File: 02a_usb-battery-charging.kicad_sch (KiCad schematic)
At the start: 20 parts, among them J3 USB4105-GF-A, J4 Conn_01x02_Socket, J5 Conn_01x03_Socket, U1 USBLC6-2SC6, U2 BQ25170JDSGR

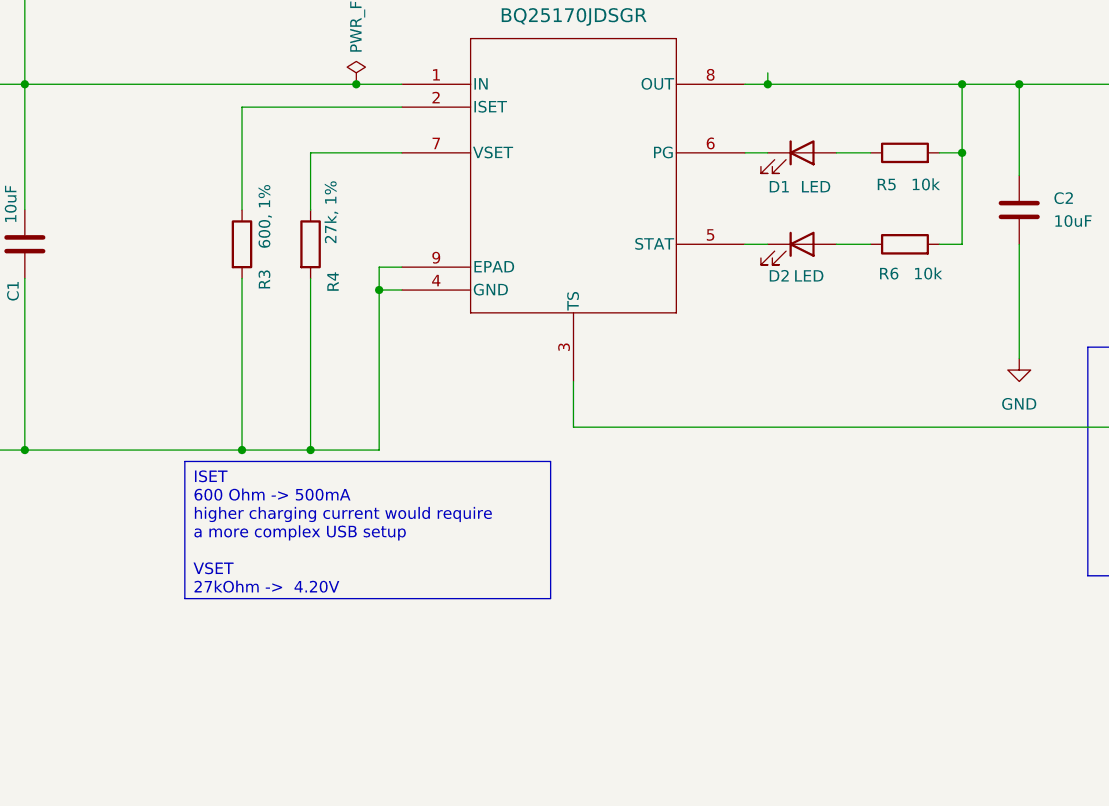
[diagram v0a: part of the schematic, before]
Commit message: Bigger Zener, improved BoM, general improvements
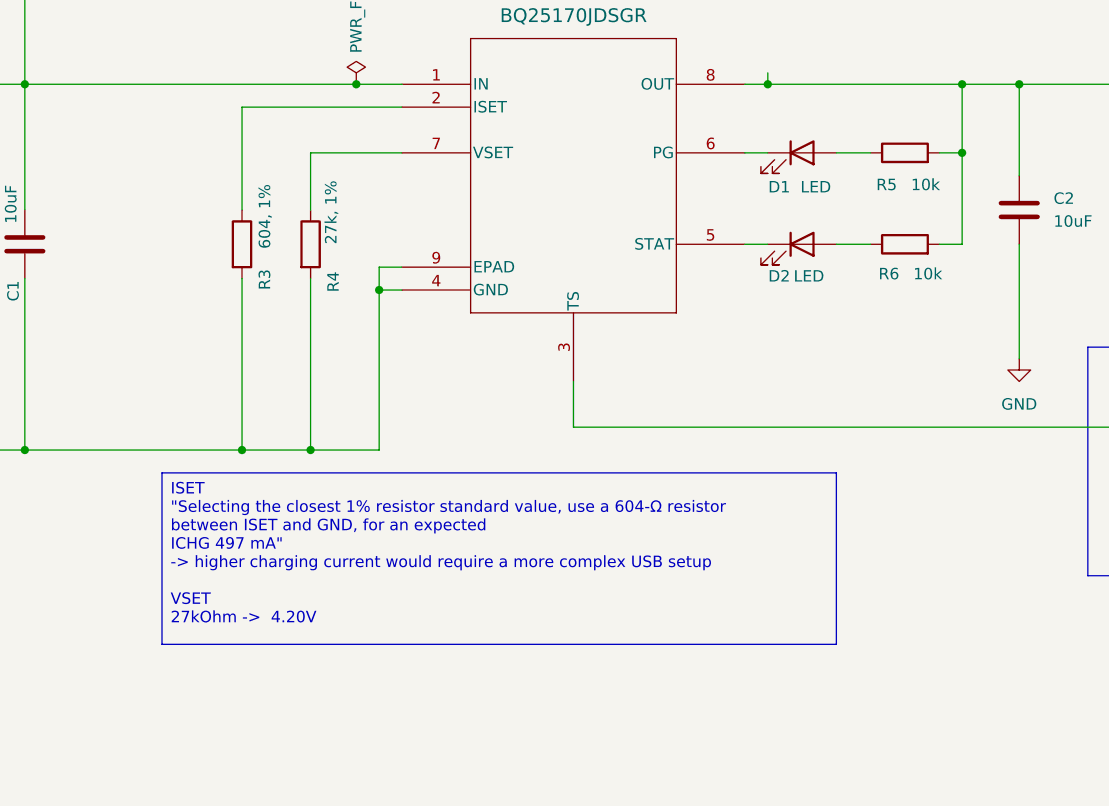
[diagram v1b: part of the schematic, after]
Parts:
- C1, C2: DigiKey (none) -> 1276-1804-1-ND; Manufacturer PartNo (none) -> CL31B106KAHNNNE
- D1: DigiKey (none) -> 732-4994-1-ND; Manufacturer PartNo (none) -> 150120YS75000
- D2: DigiKey (none) -> 732-4990-1-ND; Manufacturer PartNo (none) -> 150120GS75000
- F1: DigiKey (none) -> F3733CT-ND; Manufacturer PartNo (none) -> 1206L050/15YR
- J3: DigiKey (none) -> 2073-USB4105-GF-ACT-ND; Manufacturer PartNo (none) -> USB4105-GF-A
- J5: DigiKey (none) -> 455-1720-ND; Manufacturer PartNo (none) -> S3B-PH-K-S
- R1, R2: DigiKey (none) -> YAG3894CT-ND; Manufacturer PartNo (none) -> AC1206FR-075K1L
- R3: value 600, 1% -> 604, 1%; DigiKey (none) -> RNCP1206FTD604RCT-ND; Manufacturer PartNo (none) -> RNCP1206FTD604R
- R4: DigiKey (none) -> 311-27.0KFRCT-ND; Manufacturer PartNo (none) -> RC1206FR-0727KL
- R5, R6: DigiKey (none) -> 311-10.0KFRCT-ND; Manufacturer PartNo (none) -> RC1206FR-0710KL
- U1: Manufacturer PartNo (none) -> USBLC6-2SC6
- U2: DigiKey (none) -> 296-BQ25170JDSGRCT-ND; Manufacturer PartNo (none) -> BQ25170JDSGR

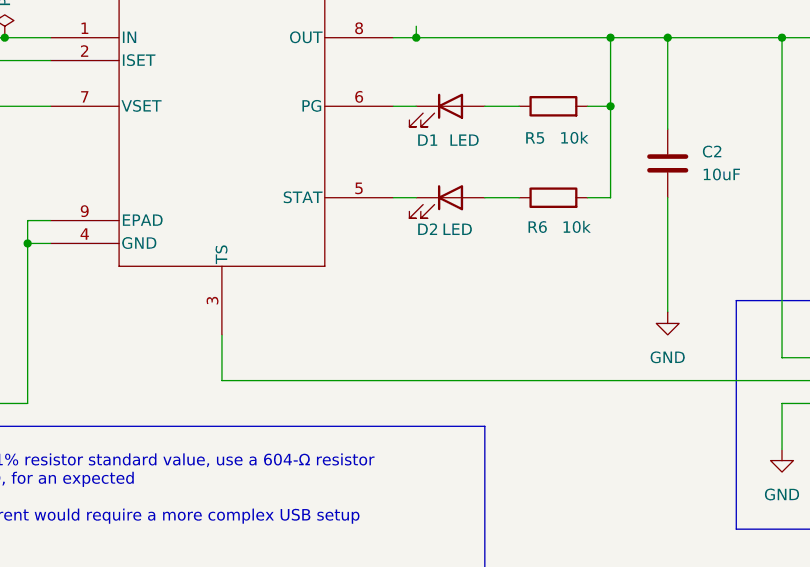
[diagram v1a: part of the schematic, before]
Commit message: Add proper charging detection, fix zener footprint
Connect the BQ25 status pin to the microcontroller for a proper
charging detection (low active).
Correct the footprint for the selected zener diode.
Somehow, the wrong footprint got assigned.
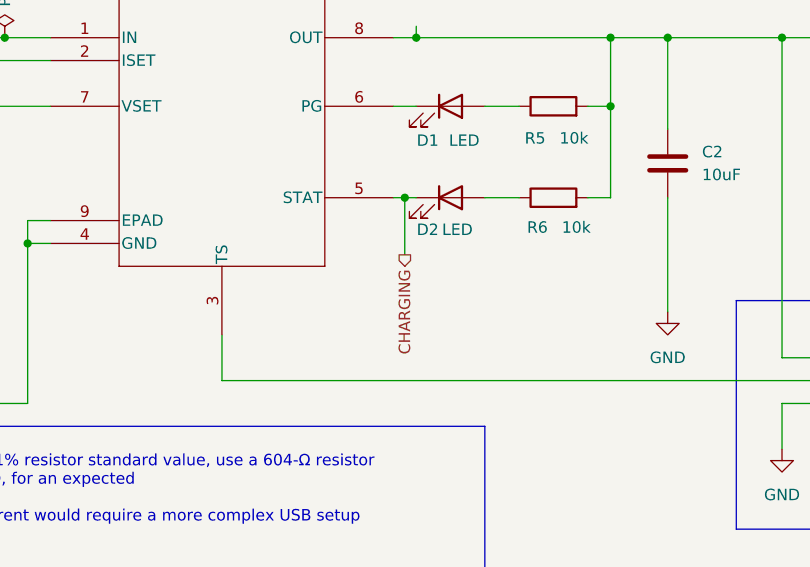
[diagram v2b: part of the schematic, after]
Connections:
- net CHARGING: now reaches D2.1 (K), U2.5 (STAT)
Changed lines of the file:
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@@
+	)
+	(junction
+		(at 189.23 93.98)
+		(diameter 0)
+		(color 0 0 0 0)
 	)
 	(junction
@@
 	(wire
 		(pts
+			(xy 189.23 93.98) (xy 190.5 93.98)
+		)
+		(stroke
+			(width 0)
+			(type default)
+		)
+	)
+	(wire
+		(pts
 			(xy 29.21 80.01) (xy 30.48 80.01)
 		)
@@
 	(wire
 		(pts
-			(xy 187.96 93.98) (xy 190.5 93.98)
+			(xy 187.96 93.98) (xy 189.23 93.98)
 		)
 		(stroke
@@
 		(pts
 			(xy 231.14 111.76) (xy 234.95 111.76)
+		)
+		(stroke
+			(width 0)
+			(type default)
+		)
+	)
+	(wire
+		(pts
+			(xy 189.23 93.98) (xy 189.23 100.33)
 		)
 		(stroke
@@
 		)
 	)
+	(hierarchical_label "CHARGING"
+		(shape output)
+		(at 189.23 100.33 270)
+		(effects
+			(font
+				(size 1.27 1.27)
+			)
+			(justify right)
+		)
+	)

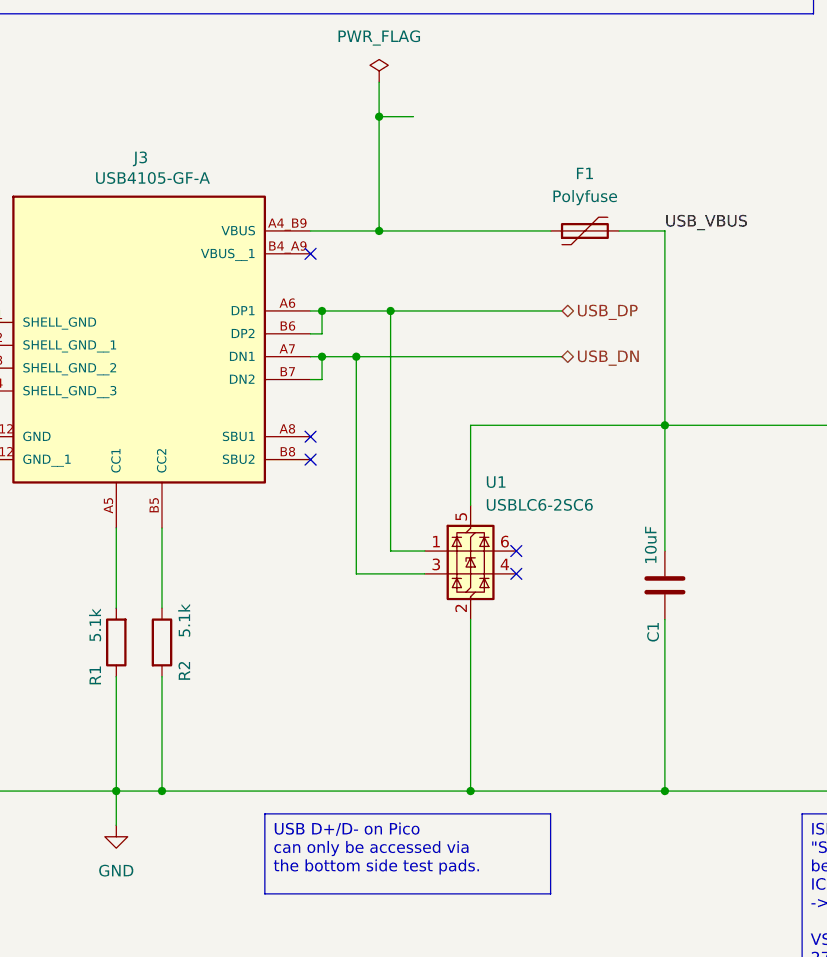
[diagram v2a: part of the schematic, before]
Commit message: Avoid using the ADC pins for anything but ADC tasks
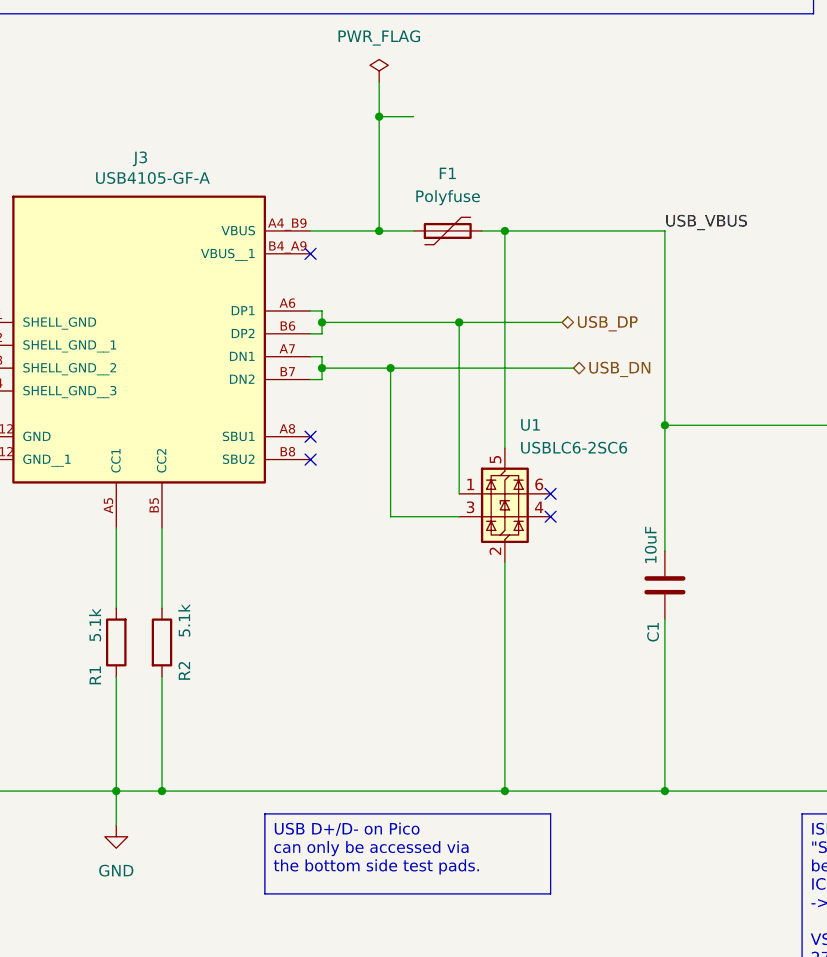
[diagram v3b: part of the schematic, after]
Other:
- moved on the sheet: F1, U1

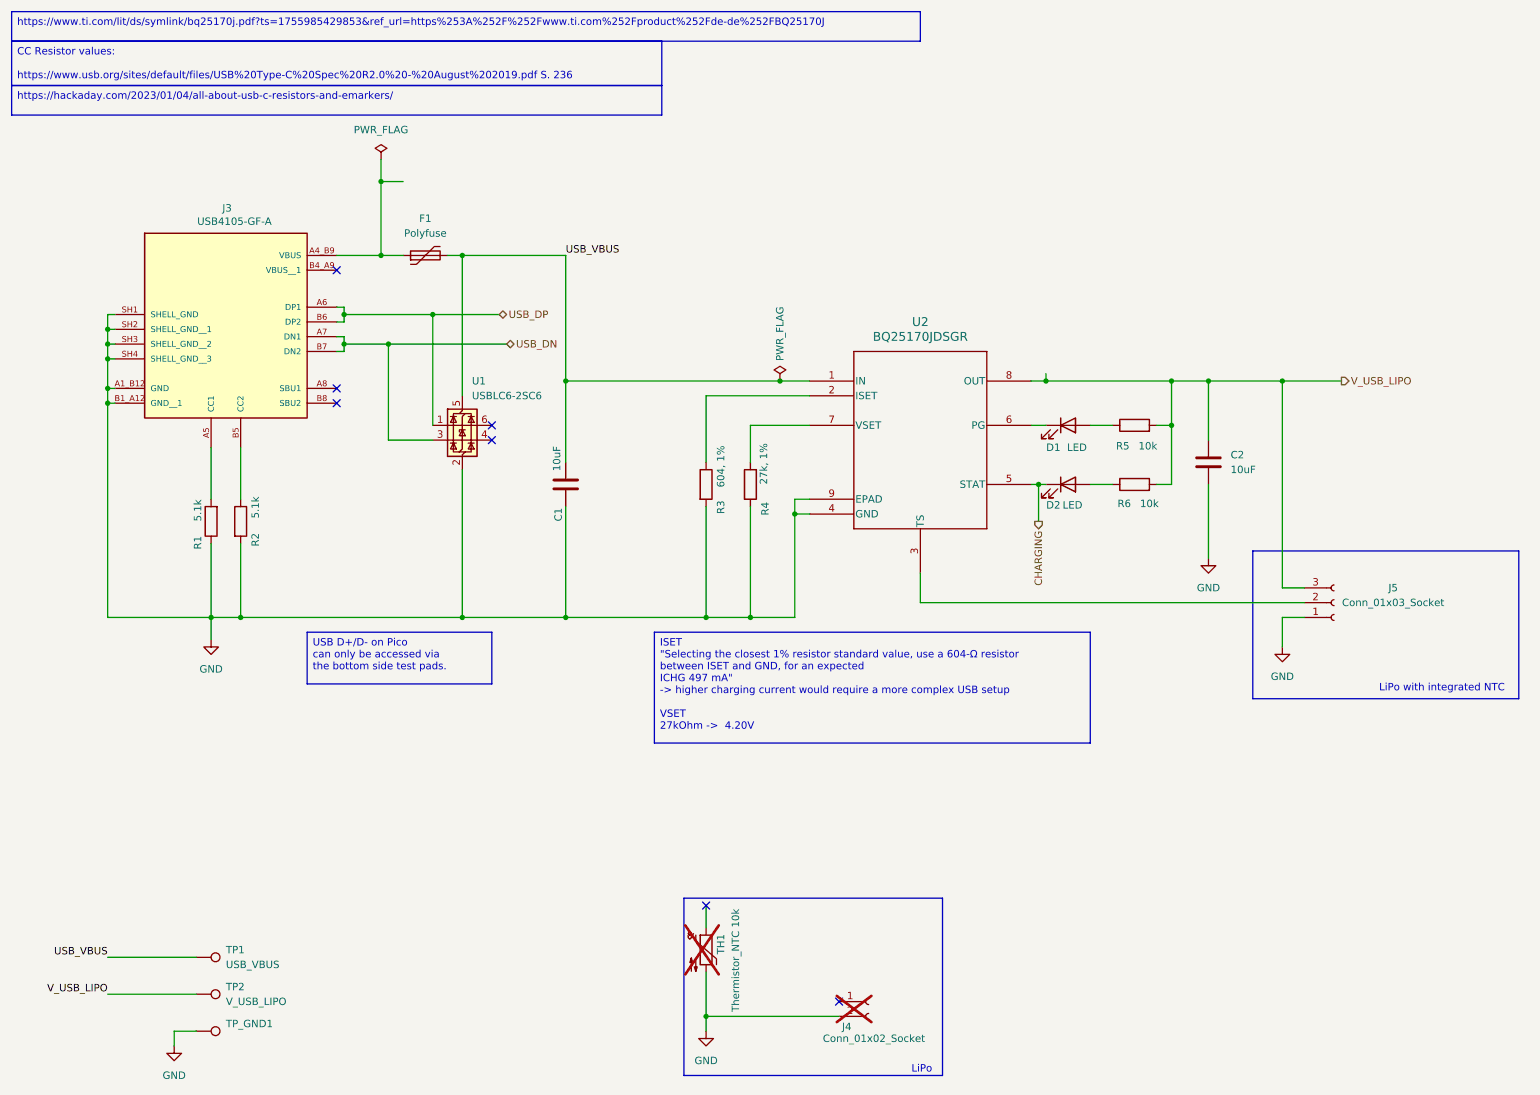
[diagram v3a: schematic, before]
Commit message: Add an voltage bypass mode when USB-C is connected
When USB-C is connected, the device should be charging, but also powered,
without taking care of the on/off button's state.
Otherwise, flashing the device via USB-C would only be
possible as long as the button is pressed which makes the usage
experience a mess and flaky.
This uses p-MOSFETs to do the switch and
a) avoid a battery voltage going to the system when USB-C is connected
b) avoid powering having both, USB-C and Micro-USB active

TODO: This adds the basic idea, routing must be fixed!
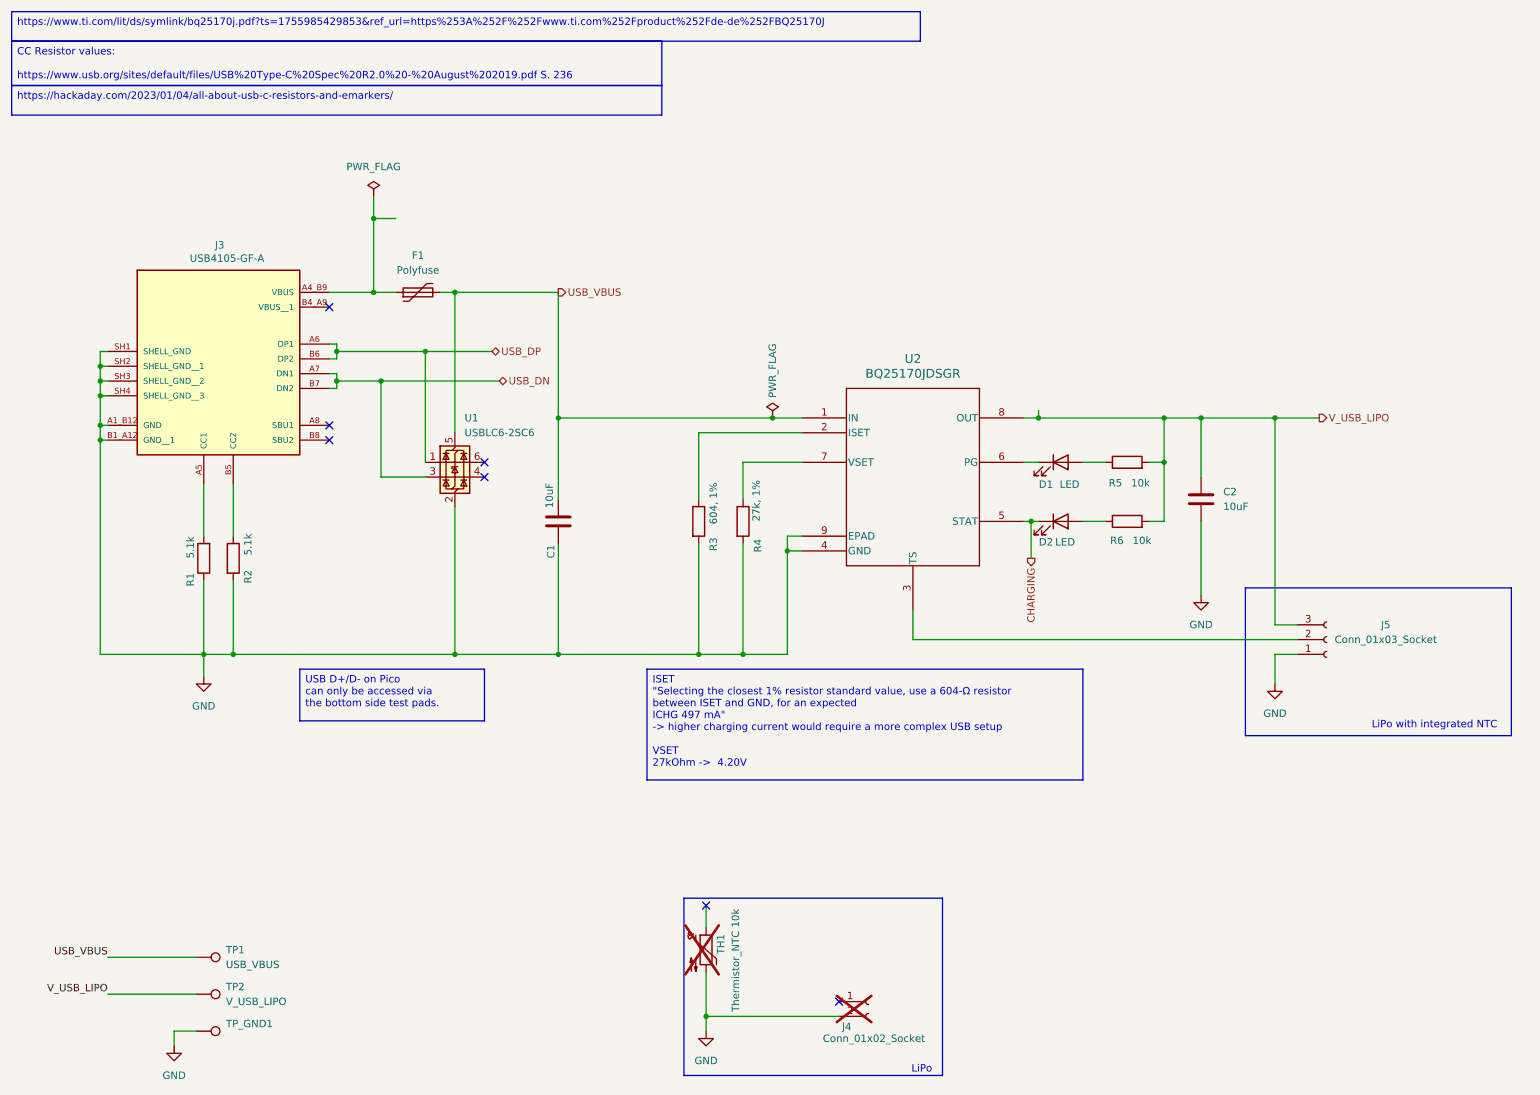
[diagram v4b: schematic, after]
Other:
- moved on the sheet: C1, C2, D1, D2, F1, J3, J5, R1, R2, R3, R4, R5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
